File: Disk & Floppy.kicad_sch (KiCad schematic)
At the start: 33 parts, among them J12 External HDD, J13 FDD Power, J7 Internal FDD, U18 74HC74, U19 74HC244, U20 74HC245, U21 74HC74, U22 74HS05, U37 DMA, U38 WD1772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

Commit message: motherboard: Routed out the bulk of the DAC section and feed latches
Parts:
- U19, U20: footprint Package_SO:SO-20_12.8x7.5mm_P1.27mm -> rhais_package-smd:SO-20_12.8x7.5mm_P1.27mm
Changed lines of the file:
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@@
 			)
 		)
-		(property "Footprint" "Package_SO:SO-20_12.8x7.5mm_P1.27mm"
+		(property "Footprint" "rhais_package-smd:SO-20_12.8x7.5mm_P1.27mm"
 			(at 88.9 63.5 0)
 			(effects
@@
 			)
 		)
-		(property "Footprint" "Package_SO:SO-20_12.8x7.5mm_P1.27mm"
+		(property "Footprint" "rhais_package-smd:SO-20_12.8x7.5mm_P1.27mm"
 			(at 88.9 127 0)
 			(effects

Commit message: motherboard: Added more footprints for parts and refined the serial comms section further
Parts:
- JP1, JP2: footprint (none) -> Jumper:SolderJumper-3_P1.3mm_Bridged12_RoundedPad1.0x1.5mm_NumberLabels
- U37: MFR (none) -> Multicomp; MPN (none) -> SPC15505; OC_FARNELL (none) -> 2678576
- U38: MFR (none) -> Multicomp; MPN (none) -> SPC15504; OC_FARNELL (none) -> 2668410
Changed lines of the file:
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@@
 			)
 		)
-		(property "Footprint" ""
+		(property "Footprint" "Jumper:SolderJumper-3_P1.3mm_Bridged12_RoundedPad1.0x1.5mm_NumberLabels"
 			(at 203.2 101.6 0)
 			(effects
@@
 			)
 		)
+		(property "MFR" "Multicomp"
+			(at 76.2 215.9 0)
+			(effects
+				(font
+					(size 1.27 1.27)
+				)
+				(hide yes)
+			)
+		)
+		(property "MPN" "SPC15505"
+			(at 76.2 215.9 0)
+			(effects
+				(font
+					(size 1.27 1.27)
+				)
+				(hide yes)
+			)
+		)
+		(property "OC_FARNELL" "2678576"
+			(at 76.2 215.9 0)
+			(effects
+				(font
+					(size 1.27 1.27)
+				)
+				(hide yes)
+			)
+		)
 		(pin "13"
 		)
@@
 			)
 		)
-		(property "Footprint" ""
+		(property "Footprint" "Jumper:SolderJumper-3_P1.3mm_Bridged12_RoundedPad1.0x1.5mm_NumberLabels"
 			(at 228.6 101.6 0)
 			(effects
@@
 			(at 152.4 218.44 0)
 			(effects
+				(font
+					(size 1.27 1.27)
+				)
+				(hide yes)
+			)
+		)
+		(property "MFR" "Multicomp"
+			(at 152.4 218.44 0)
+			(effects
+				(font
+					(size 1.27 1.27)
+				)
+				(hide yes)
+			)
+		)
+		(property "MPN" "SPC15504"
+			(at 152.4 218.44 0)
+			(effects
+				(font
+					(size 1.27 1.27)
+				)
+				(hide yes)
+			)
+		)
+		(property "OC_FARNELL" "2668410"
+			(at 152.4 218.44 0)
+			(effects

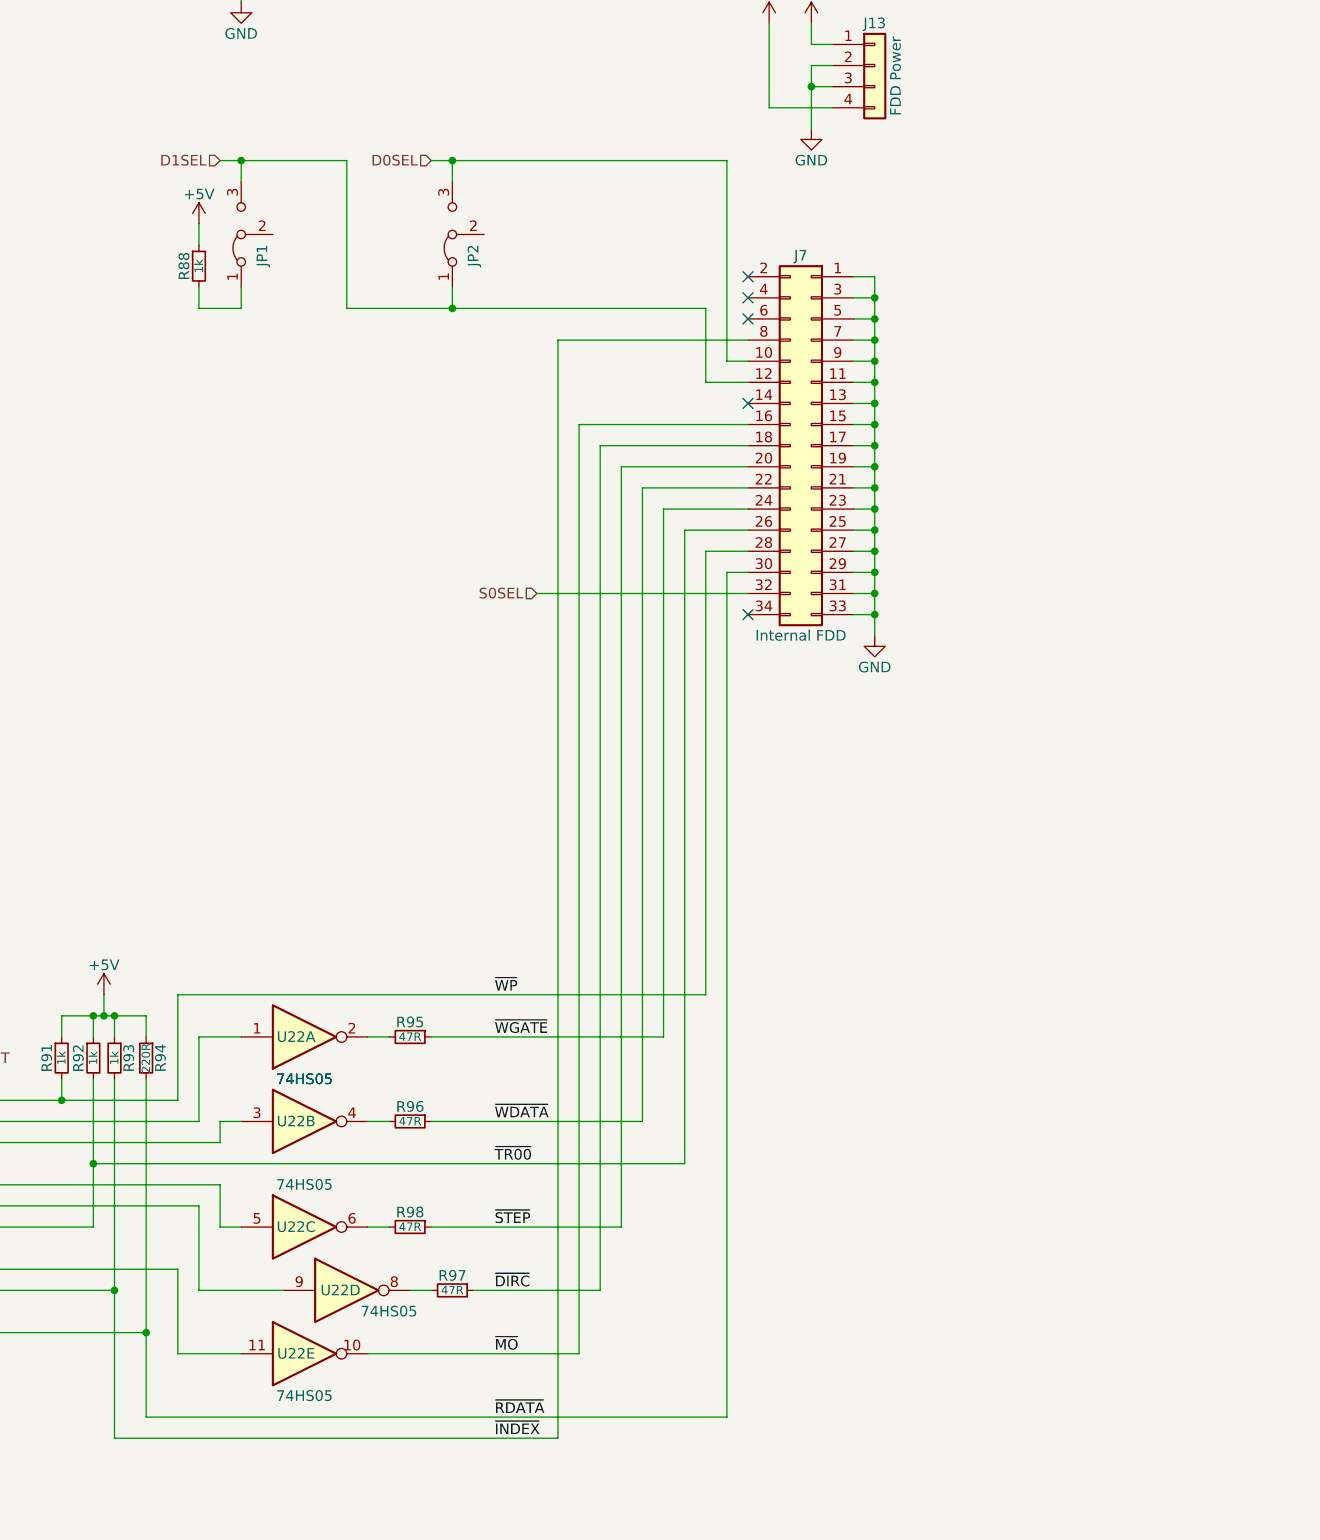
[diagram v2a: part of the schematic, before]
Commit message: motherboard: Added the external keyboard connector and put the FDD interface into probably its final resting spot
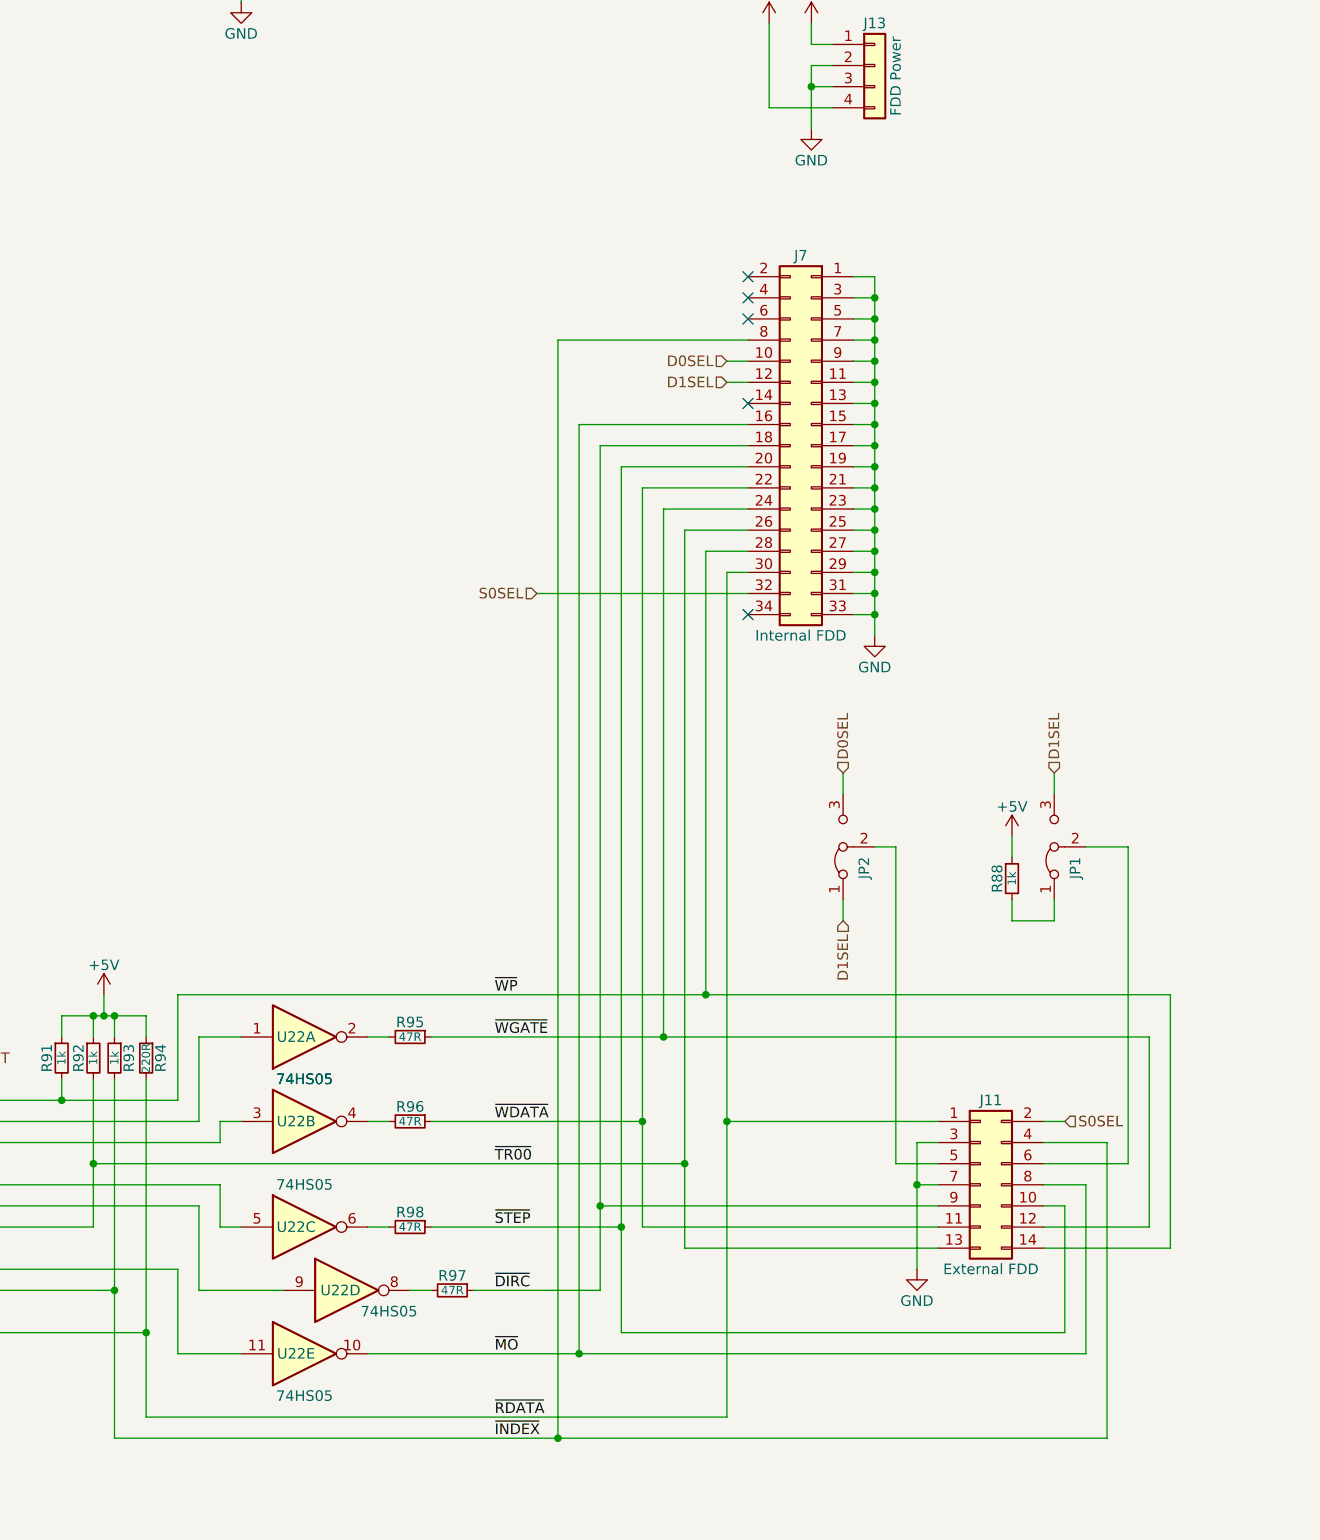
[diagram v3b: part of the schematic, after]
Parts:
- added J11: External FDD, Connector_PinHeader_2.54mm:PinHeader_2x07_P2.54mm_Horizontal, symbol Connector_Generic:Conn_02x07_Odd_Even
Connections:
- net GND: now also J11.3 (Pin_3), J11.7 (Pin_7)
- net S0SEL: now also J11.2 (Pin_2)
- net ~{DIRC}: now also J11.9 (Pin_9)
- net ~{INDEX}: now also J11.4 (Pin_4)
- net ~{MO}: now also J11.8 (Pin_8)
- net ~{RDATA}: now also J11.1 (Pin_1)
- net ~{STEP}: now also J11.10 (Pin_10)
- net ~{TR00}: now also J11.13 (Pin_13)
- net ~{WDATA}: now also J11.11 (Pin_11)
- net ~{WGATE}: now also J11.12 (Pin_12)
- net ~{WP}: now also J11.14 (Pin_14)
- net at JP1.2 (C): now also J11.6 (Pin_6)
- net at JP2.2 (C): now also J11.5 (Pin_5)
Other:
- moved on the sheet: JP1, JP2, R88

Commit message: motherboard: Routed in the external floppy interface connector
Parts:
- J11: footprint Connector_PinHeader_2.54mm:PinHeader_2x07_P2.54mm_Horizontal -> rhais_connector-pinheader:PinHeader_2x07_P2.54mm_Horizontal
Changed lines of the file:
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@@
 			)
 		)
-		(property "Footprint" "Connector_PinHeader_2.54mm:PinHeader_2x07_P2.54mm_Horizontal"
+		(property "Footprint" "rhais_connector-pinheader:PinHeader_2x07_P2.54mm_Horizontal"
 			(at 292.1 215.9 0)
 			(effects
@@
 			(at 292.1 215.9 0)
 			(effects
+				(font
+					(size 1.27 1.27)
+				)
+				(hide yes)
+			)
+		)
+		(property "MFR" ""
+			(at 292.1 215.9 0)
+			(effects
+				(font
+					(size 1.27 1.27)
+				)
+				(hide yes)
+			)
+		)
+		(property "MPN" ""
+			(at 292.1 215.9 0)
+			(effects
+				(font
+					(size 1.27 1.27)
+				)
+				(hide yes)
+			)
+		)
+		(property "OC_FARNELL" ""
+			(at 292.1 215.9 0)
+			(effects

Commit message: motherboard: Sorted out a portion of the HDD interface
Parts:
- added C122, C123: 100n, rhais_rcl:C0603, symbol Device:C_Small
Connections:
- net +5V: now also C122.1, C123.1
- net GND: now also U21.10 (~{S}), U21.11 (C), U21.12 (D), U21.13 (~{R}), C122.2, C123.2
- net at U19.13 (I1b), U38.3 (A0): now also U37.26 (CA1); no longer U37.28 (CA1)
- no-connect marks 8 -> 10

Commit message: motherboard: Sorted some of the clock generation circuitry out
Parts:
- removed U21: 74HC74, rhais_package-smd:SO-14_3.9x8.65mm_P1.27mm, symbol 74xx:74LS74
- added U4: 74HC74, rhais_package-smd:SO-14_3.9x8.65mm_P1.27mm, symbol 74xx:74HC74
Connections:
- net +5V: now also U4.14 (VCC), U4.4 (~{S})
- net CLK8: now also U4.3 (C)
- net GND: now also U4.7 (GND)
- net at U20.19 (CE): now also U4.6 (~{Q})
- new net: U4.1 (~{R}), U4.2 (D)
- no-connect marks 10 -> 8

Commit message: motherboard: Sorted out the secondary clock source
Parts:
- added C124: 100n, rhais_rcl:C0603, symbol Device:C_Small
- X1: footprint rhais_osc:SMD2520 -> rhais_osc:SMD3225; MFR TXC -> Microchip; MPN (none) -> DSC8004CI2; OC_DIGIKEY (none) -> 576-4680-ND
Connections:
- net +5V: no longer X1.4 (Vdd)
- net GND: now also C124.2
- net +3V3: now reaches X1.1 (EN)
- net +3V3: now also X1.4 (Vdd), C124.1
